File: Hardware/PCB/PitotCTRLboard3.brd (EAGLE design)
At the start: 17.8 x 75.1 mm, 67 parts, among them J1 2201778-1, U1 STM32F405RGT6, U2 MAX1595EUA33+

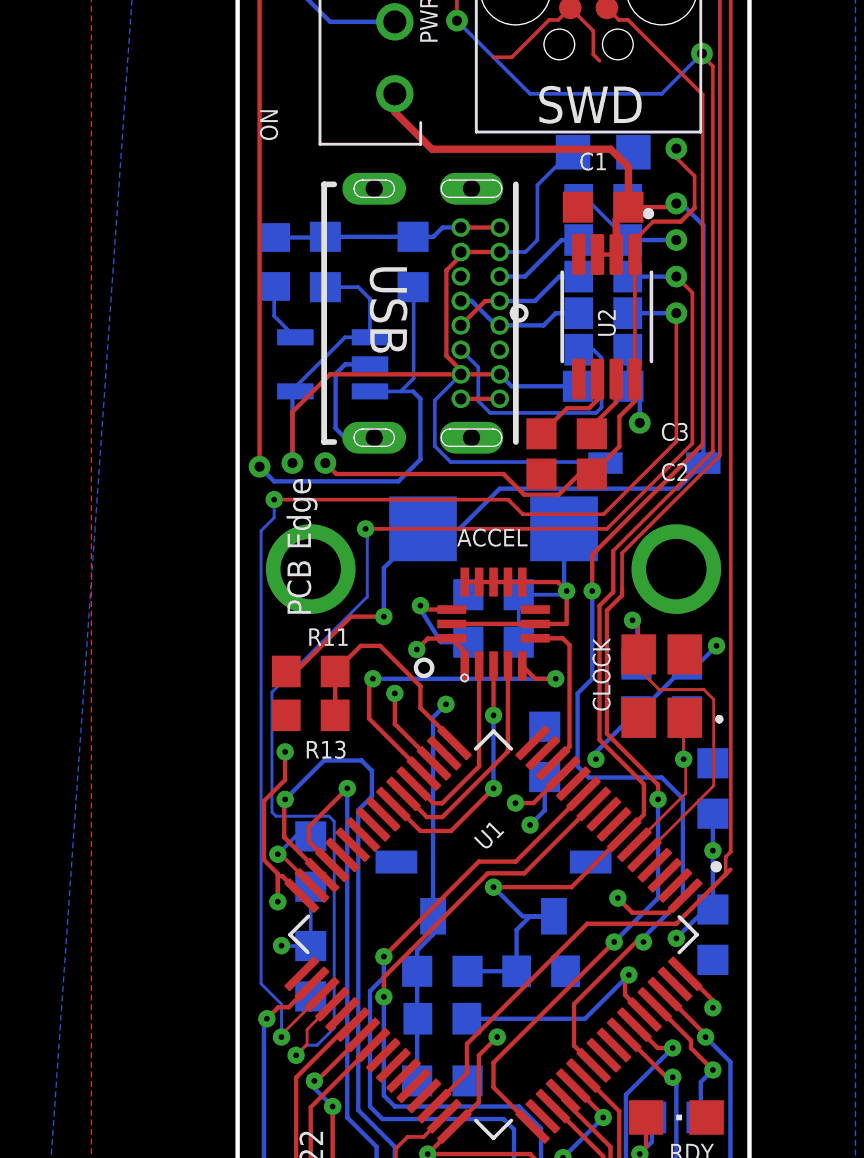
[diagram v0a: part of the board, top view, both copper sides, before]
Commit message: fix usb-c position
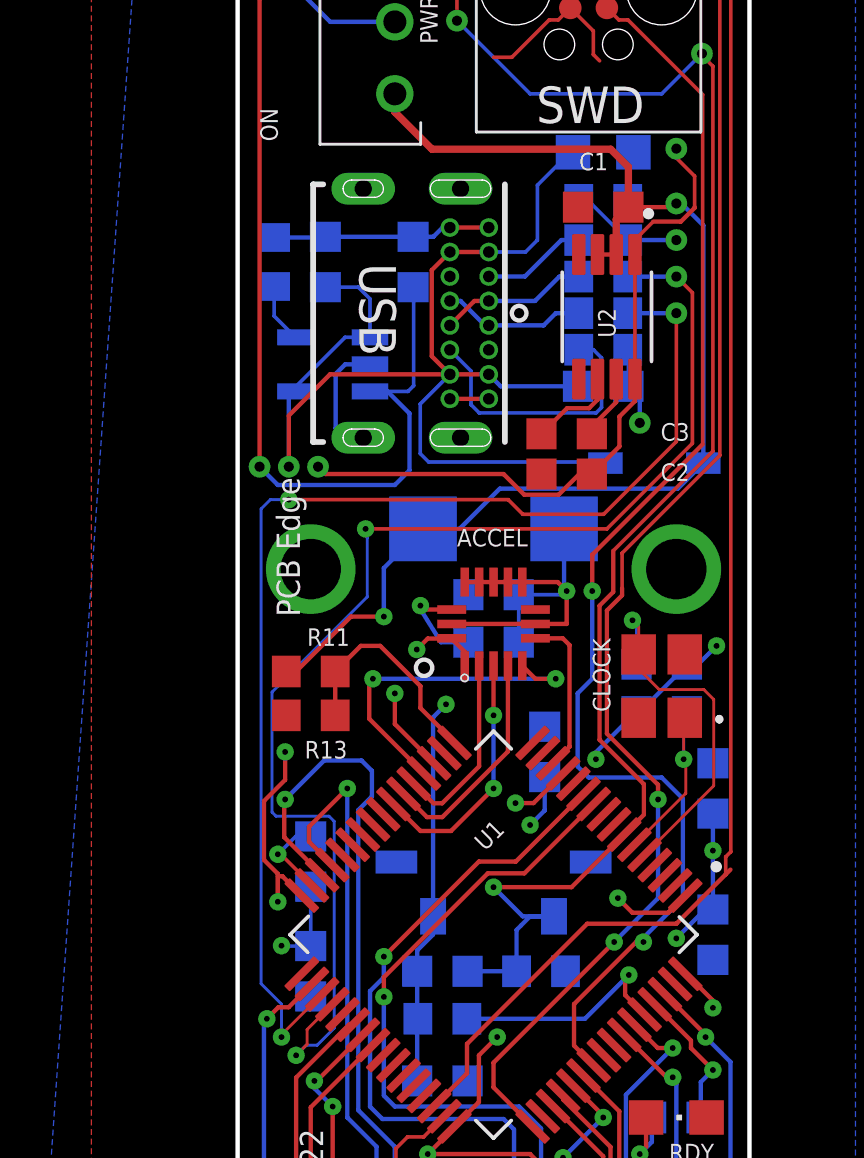
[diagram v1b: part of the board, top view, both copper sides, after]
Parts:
- moved USB 0.38 mm to (-4.19, 21.6)
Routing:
- net +5V: track 41.7 -> 43.3 mm
- net GND: track 94.1 -> 93.1 mm
- net N$52: track 4.62 -> 5.62 mm

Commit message: bug fix
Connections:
- net GND: now also TEMP.16
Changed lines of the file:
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@@
 <drawing>
 <settings>
-<setting alwaysvectorfont="yes"/>
+<setting alwaysvectorfont="no"/>
 <setting verticaltext="up"/>
 </settings>
@@
 <wire x1="2.413" y1="11.811" x2="0.875" y2="11.811" width="0.127" layer="16"/>
 <wire x1="0.875" y1="11.811" x2="0.875" y2="10.16" width="0.127" layer="16"/>
+<contactref element="TEMP" pad="16"/>
 </signal>
 <signal name="+3V3">
